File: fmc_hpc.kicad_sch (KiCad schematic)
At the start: 28 parts

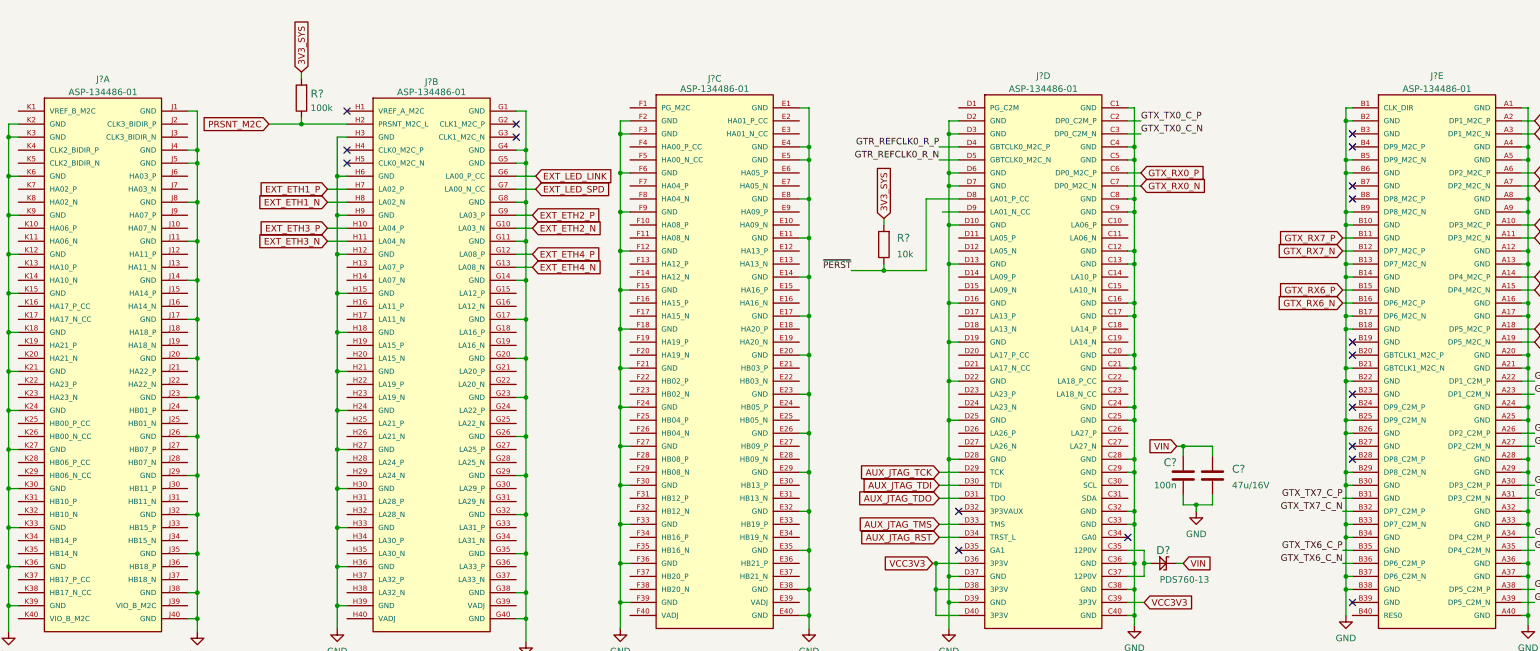
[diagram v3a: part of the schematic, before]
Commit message: Reconnect FMC signals to new socket, and JTAG to new connector
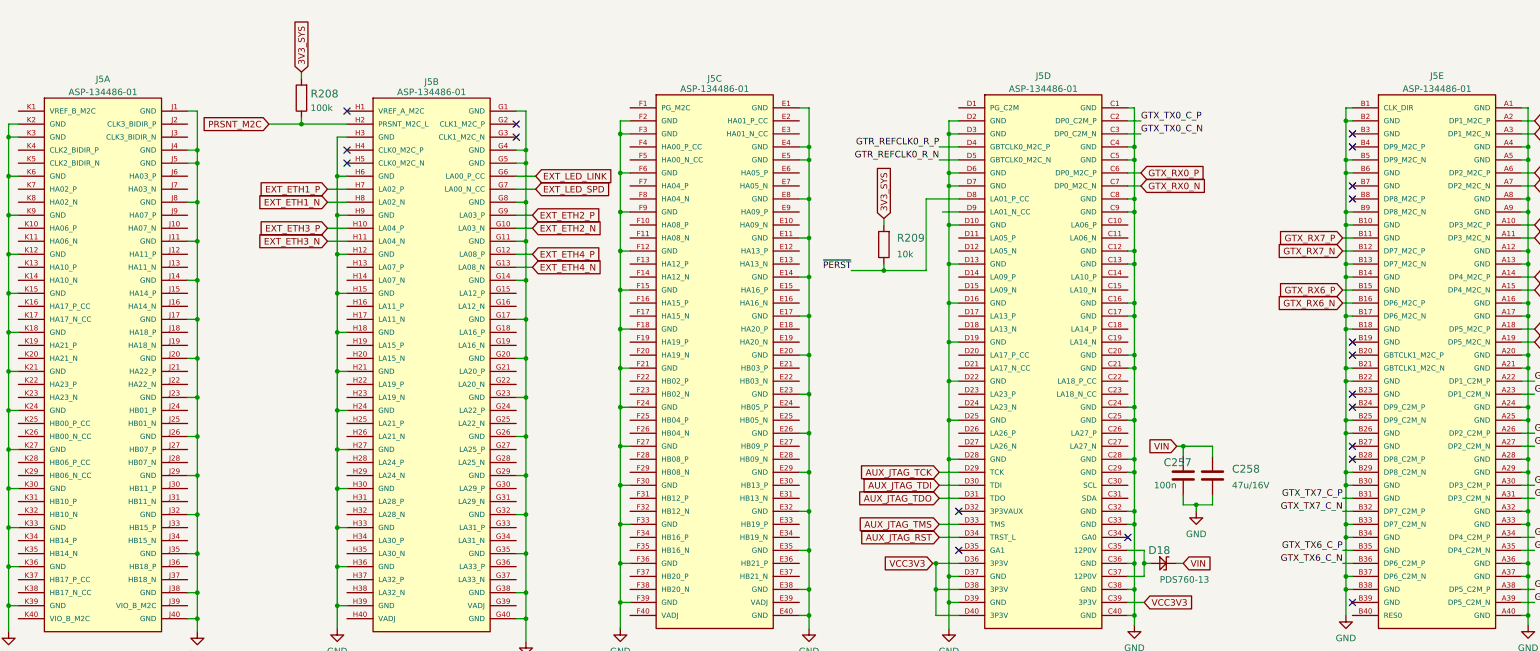
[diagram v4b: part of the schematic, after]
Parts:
- gave numbers to parts that had none: 6
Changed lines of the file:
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@@
   (symbol (lib_id "power:GND") (at 288.925 165.735 0) (unit 1)
     (in_bom yes) (on_board yes) (fields_autoplaced)
-    (property "Reference" "#PWR?" (id 0) (at 288.925 172.085 0)
+    (property "Reference" "#PWR0348" (id 0) (at 288.925 172.085 0)
       (effects (font (size 1.27 1.27)) hide)
     )
@@
   (symbol (lib_id "power:GND") (at 27.94 168.91 0) (unit 1)
     (in_bom yes) (on_board yes) (fields_autoplaced)
-    (property "Reference" "#PWR?" (id 0) (at 27.94 175.26 0)
+    (property "Reference" "#PWR0351" (id 0) (at 27.94 175.26 0)
       (effects (font (size 1.27 1.27)) hide)
     )
@@
   (symbol (lib_id "power:GND") (at 147.32 168.275 0) (unit 1)
     (in_bom yes) (on_board yes) (fields_autoplaced)
-    (property "Reference" "#PWR?" (id 0) (at 147.32 174.625 0)
+    (property "Reference" "#PWR0353" (id 0) (at 147.32 174.625 0)
       (effects (font (size 1.27 1.27)) hide)
     )
@@
   (symbol (lib_id "antmicroFMCConnectors:ASP-134486-01") (at 110.49 115.57 0) (unit 2)
     (in_bom yes) (on_board yes)
-    (property "Reference" "J?" (id 0) (at 110.49 61.595 0))
+    (property "Reference" "J5" (id 0) (at 110.49 61.595 0))
     (property "Value" "ASP-134486-01" (id 1) (at 110.49 63.6071 0))
     (property "Footprint" "antmicro-footprints:SAMTEC_ASP-134486-01" (id 2) (at 99.06 173.99 0)
@@
   (symbol (lib_id "power:GND") (at 247.65 167.64 0) (unit 1)
     (in_bom yes) (on_board yes) (fields_autoplaced)
-    (property "Reference" "#PWR?" (id 0) (at 247.65 173.99 0)
+    (property "Reference" "#PWR0347" (id 0) (at 247.65 173.99 0)
       (effects (font (size 1.27 1.27)) hide)
     )
@@
   (symbol (lib_id "power:GND") (at 184.15 168.275 0) (unit 1)
     (in_bom yes) (on_board yes) (fields_autoplaced)
-    (property "Reference" "#PWR?" (id 0) (at 184.15 174.625 0)
+    (property "Reference" "#PWR0349" (id 0) (at 184.15 174.625 0)
       (effects (font (size 1.27 1.27)) hide)
     )
@@
   (symbol (lib_id "antmicroFMCConnectors:ASP-134486-01") (at 306.705 114.935 0) (unit 5)
     (in_bom yes) (on_board yes) (fields_autoplaced)
-    (property "Reference" "J?" (id 0) (at 306.705 60.4352 0))
+    (property "Reference" "J5" (id 0) (at 306.705 60.4352 0))
     (property "Value" "ASP-134486-01" (id 1) (at 306.705 62.9721 0))
     (property "Footprint" "antmicro-footprints:SAMTEC_ASP-134486-01" (id 2) (at 295.275 173.355 0)
@@
   (symbol (lib_id "power:GND") (at 92.075 168.275 0) (unit 1)
     (in_bom yes) (on_board yes) (fields_autoplaced)
-    (property "Reference" "#PWR?" (id 0) (at 92.075 174.625 0)
+    (property "Reference" "#PWR0350" (id 0) (at 92.075 174.625 0)
       (effects (font (size 1.27 1.27)) hide)
     )
@@
   (symbol (lib_id "power:GND") (at 259.715 145.415 0) (unit 1)
     (in_bom yes) (on_board yes) (fields_autoplaced)
-    (property "Reference" "#PWR?" (id 0) (at 259.715 151.765 0)
+    (property "Reference" "#PWR0345" (id 0) (at 259.715 151.765 0)
       (effects (font (size 1.27 1.27)) hide)
     )
@@
   (symbol (lib_id "power:GND") (at 211.455 168.275 0) (unit 1)
     (in_bom yes) (on_board yes) (fields_autoplaced)
-    (property "Reference" "#PWR?" (id 0) (at 211.455 174.625 0)
+    (property "Reference" "#PWR0346" (id 0) (at 211.455 174.625 0)
       (effects (font (size 1.27 1.27)) hide)
     )
@@
   (symbol (lib_id "antmicroResistors0402:R_10k_0402") (at 198.755 93.345 90) (unit 1)
     (in_bom yes) (on_board yes) (fields_autoplaced)
-    (property "Reference" "R?" (id 0) (at 201.295 92.075 90)
+    (property "Reference" "R209" (id 0) (at 201.295 92.075 90)
       (effects (font (size 1.524 1.524)) (justify right))
     )
@@
   (symbol (lib_id "power:GND") (at 324.485 167.64 0) (unit 1)
     (in_bom yes) (on_board yes) (fields_autoplaced)
-    (property "Reference" "#PWR?" (id 0) (at 324.485 173.99 0)
+    (property "Reference" "#PWR0344" (id 0) (at 324.485 173.99 0)
       (effects (font (size 1.27 1.27)) hide)
     )
@@
   (symbol (lib_id "antmicroFMCConnectors:ASP-134486-01") (at 165.735 114.935 0) (unit 3)
     (in_bom yes) (on_board yes)
-    (property "Reference" "J?" (id 0) (at 165.735 60.96 0))
+    (property "Reference" "J5" (id 0) (at 165.735 60.96 0))
     (property "Value" "ASP-134486-01" (id 1) (at 165.735 62.9721 0))
     (property "Footprint" "antmicro-footprints:SAMTEC_ASP-134486-01" (id 2) (at 154.305 173.355 0)
@@
   (symbol (lib_id "antmicroFMCConnectors:ASP-134486-01") (at 46.355 115.57 0) (unit 1)
     (in_bom yes) (on_board yes) (fields_autoplaced)
-    (property "Reference" "J?" (id 0) (at 46.355 61.0702 0))
+    (property "Reference" "J5" (id 0) (at 46.355 61.0702 0))
     (property "Value" "ASP-134486-01" (id 1) (at 46.355 63.6071 0))
     (property "Footprint" "antmicro-footprints:SAMTEC_ASP-134486-01" (id 2) (at 34.925 173.99 0)
@@
   (symbol (lib_id "power:GND") (at 128.905 170.815 0) (unit 1)
     (in_bom yes) (on_board yes) (fields_autoplaced)
-    (property "Reference" "#PWR?" (id 0) (at 128.905 177.165 0)
+    (property "Reference" "#PWR0354" (id 0) (at 128.905 177.165 0)
       (effects (font (size 1.27 1.27)) hide)
     )
@@
   (symbol (lib_id "antmicroCapacitorsmisc:C_100n_0201") (at 257.175 138.43 0) (unit 1)
     (in_bom yes) (on_board yes)
-    (property "Reference" "C?" (id 0) (at 253.365 135.89 0)
+    (property "Reference" "C257" (id 0) (at 253.365 135.89 0)
       (effects (font (size 1.524 1.524)) (justify left))
     )
@@
   (symbol (lib_id "antmicroResistors0402:R_100k_0402") (at 85.09 64.77 90) (unit 1)
     (in_bom yes) (on_board yes) (fields_autoplaced)
-    (property "Reference" "R?" (id 0) (at 86.868 63.9354 90)
+    (property "Reference" "R208" (id 0) (at 86.868 63.9354 90)
       (effects (font (size 1.524 1.524)) (justify right))
     )
@@
   (symbol (lib_id "data-center-dram-tester:PDS760-13") (at 253.365 155.575 270) (unit 1)
     (in_bom yes) (on_board yes)
-    (property "Reference" "D?" (id 0) (at 254.635 153.035 90)
+    (property "Reference" "D18" (id 0) (at 254.635 153.035 90)
       (effects (font (size 1.524 1.524)) (justify right))
     )
@@
   (symbol (lib_id "power:GND") (at 64.77 168.91 0) (unit 1)
     (in_bom yes) (on_board yes) (fields_autoplaced)
-    (property "Reference" "#PWR?" (id 0) (at 64.77 175.26 0)
+    (property "Reference" "#PWR0352" (id 0) (at 64.77 175.26 0)
       (effects (font (size 1.27 1.27)) hide)
     )
@@
   (symbol (lib_id "antmicroCapacitorsmisc:C_47u_16V_1206") (at 262.89 138.43 0) (unit 1)
     (in_bom yes) (on_board yes) (fields_autoplaced)
-    (property "Reference" "C?" (id 0) (at 266.7 137.16 0)
+    (property "Reference" "C258" (id 0) (at 266.7 137.16 0)
       (effects (font (size 1.524 1.524)) (justify left))
     )
@@
   (symbol (lib_id "antmicroFMCConnectors:ASP-134486-01") (at 229.87 114.935 0) (unit 4)
     (in_bom yes) (on_board yes) (fields_autoplaced)
-    (property "Reference" "J?" (id 0) (at 229.87 60.4352 0))
+    (property "Reference" "J5" (id 0) (at 229.87 60.4352 0))
     (property "Value" "ASP-134486-01" (id 1) (at 229.87 62.9721 0))
     (property "Footprint" "antmicro-footprints:SAMTEC_ASP-134486-01" (id 2) (at 218.44 173.355 0)

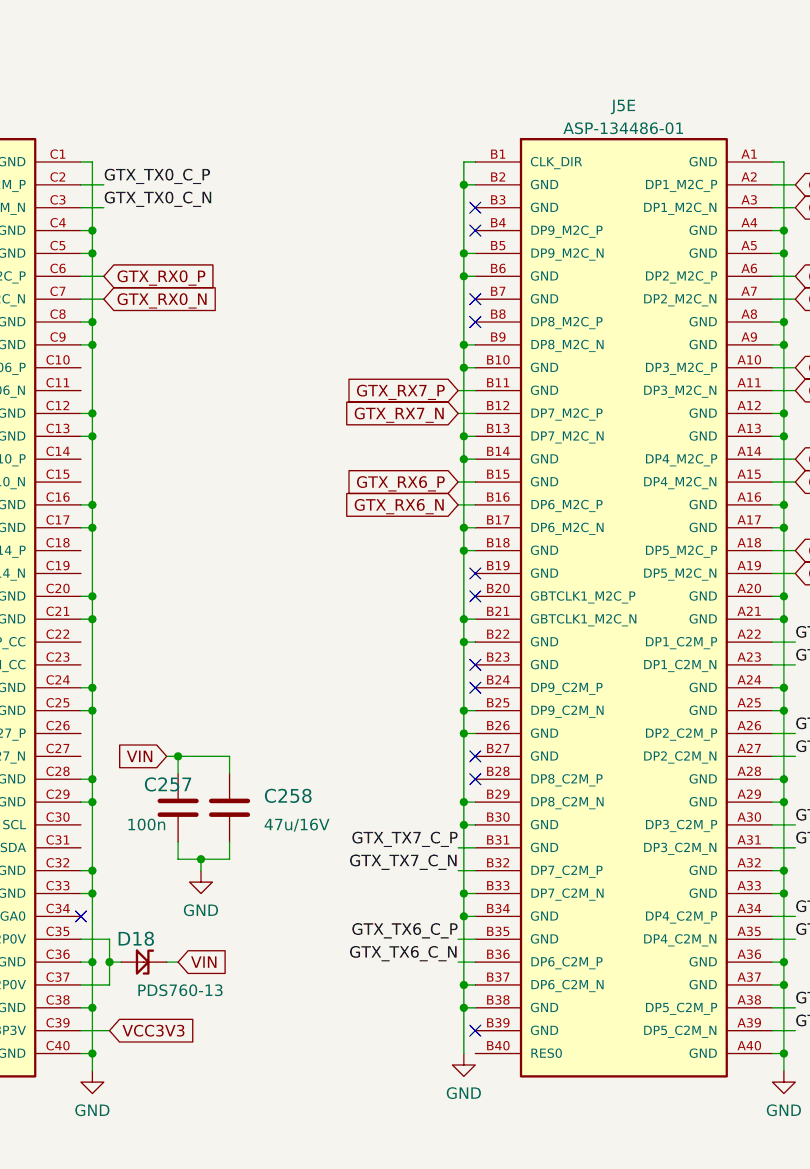
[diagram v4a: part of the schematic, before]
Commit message: All components inside the board area, fix FMC column B shift on schematic, add PCIe layer dependent rules
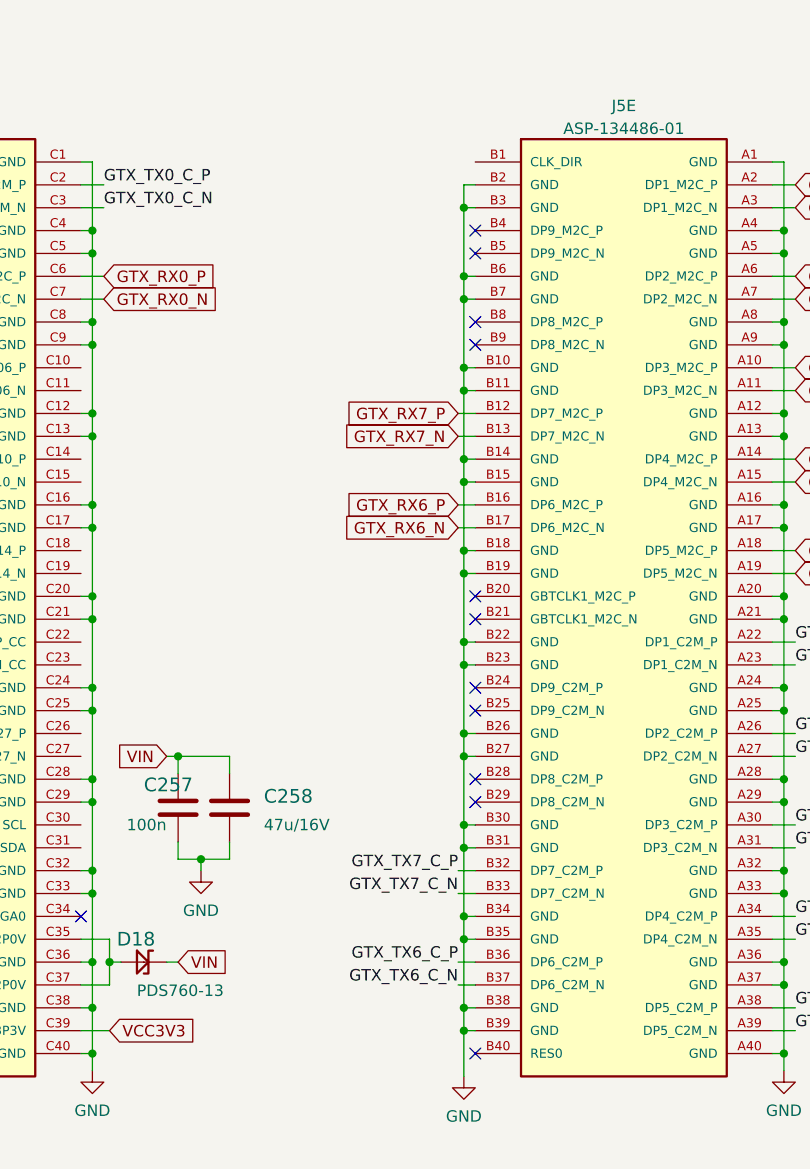
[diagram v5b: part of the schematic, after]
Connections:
- net GND: now also J5.B11 (GND), J5.B15 (GND), J5.B19 (GND), J5.B23 (GND), J5.B27 (GND), J5.B3 (GND), J5.B31 (GND), J5.B35 (GND), J5.B39 (GND), J5.B7 (GND); no longer J5.B1 (CLK_DIR), J5.B13 (DP7_M2C_N), J5.B17 (DP6_M2C_N), J5.B21 (GBTCLK1_M2C_N), J5.B25 (DP9_C2M_N), J5.B29 (DP8_C2M_N), J5.B33 (DP7_C2M_N), J5.B37 (DP6_C2M_N), J5.B5 (DP9_M2C_N), J5.B9 (DP8_M2C_N)
- net GTX_RX6_N: now also J5.B17 (DP6_M2C_N); no longer J5.B16 (DP6_M2C_P)
- net GTX_RX6_P: now also J5.B16 (DP6_M2C_P); no longer J5.B15 (GND)
- net GTX_RX7_N: now also J5.B13 (DP7_M2C_N); no longer J5.B12 (DP7_M2C_P)
- net GTX_RX7_P: now also J5.B12 (DP7_M2C_P); no longer J5.B11 (GND)
- net GTX_TX6_C_N: now also J5.B37 (DP6_C2M_N); no longer J5.B36 (DP6_C2M_P)
- net GTX_TX6_C_P: now also J5.B36 (DP6_C2M_P); no longer J5.B35 (GND)
- net GTX_TX7_C_N: now also J5.B33 (DP7_C2M_N); no longer J5.B32 (DP7_C2M_P)
- net GTX_TX7_C_P: now also J5.B32 (DP7_C2M_P); no longer J5.B31 (GND)

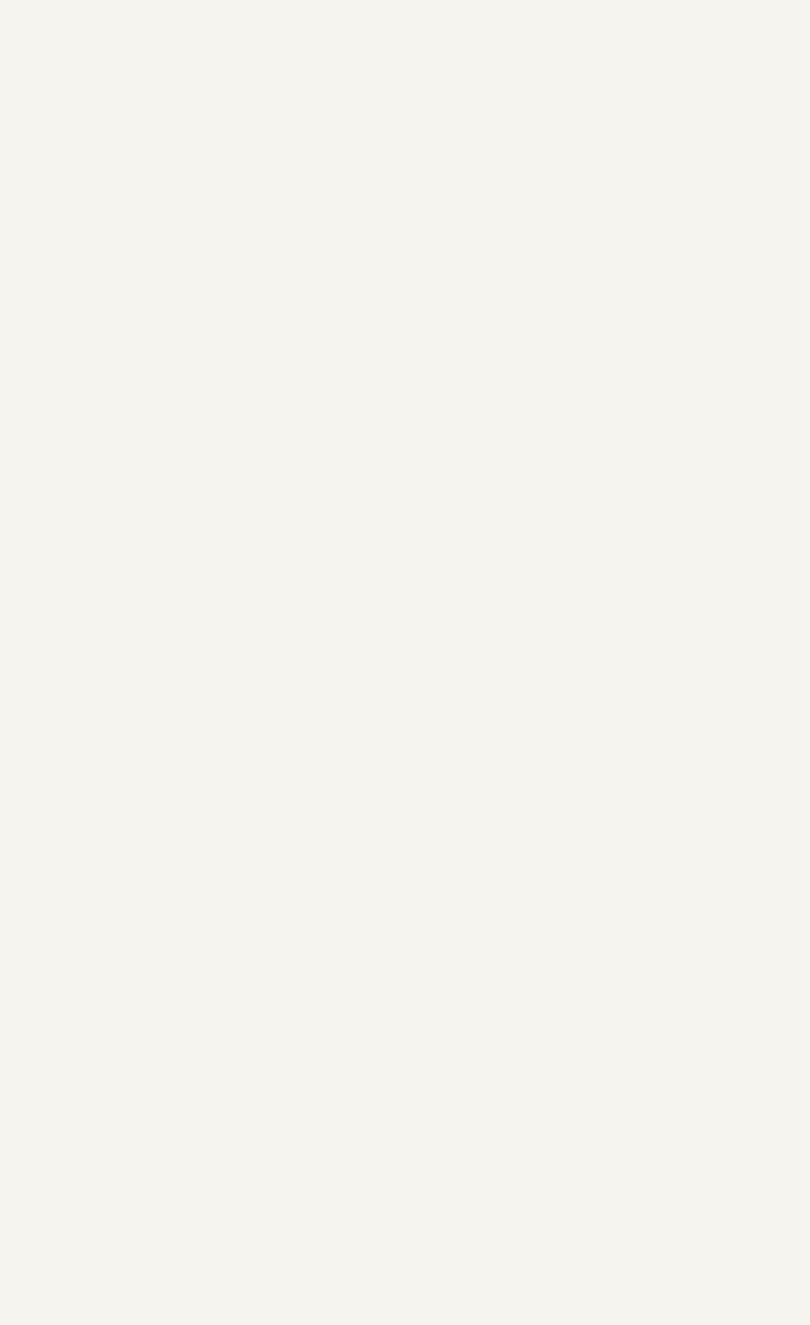
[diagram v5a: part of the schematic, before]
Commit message: Improve mechanical concept
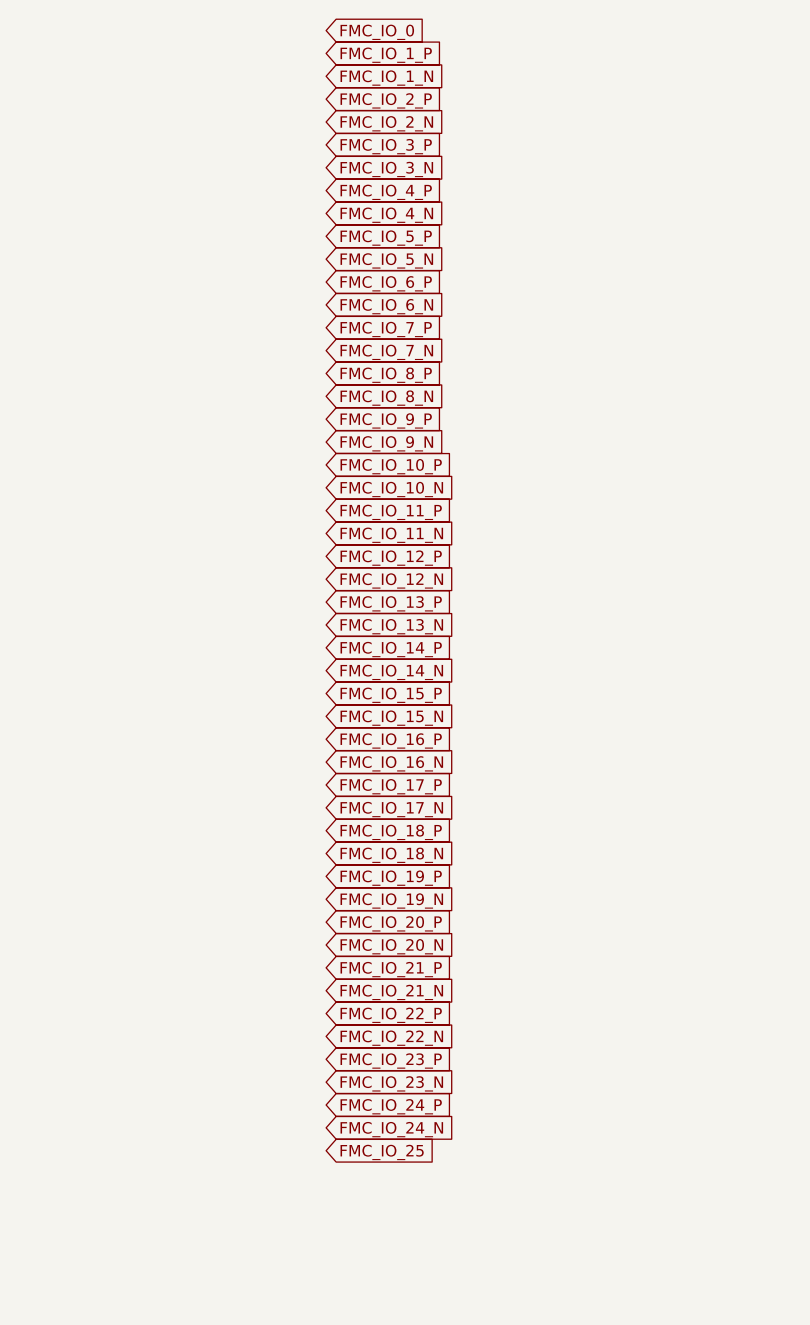
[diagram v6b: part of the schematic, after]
